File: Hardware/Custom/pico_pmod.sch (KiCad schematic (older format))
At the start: 31 parts, among them J1 Conn_02x06_Odd_Even, J2 Conn_02x06_Odd_Even, J3 Conn_02x06_Odd_Even, J4 USB_C_Receptacle_USB2.0, J5 Conn_01x04, SW1 SW_Push, SW2 SW_Push, U1 RP2040, U2 W25Q128JVS, U3 NCP1117-3.3_SOT223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

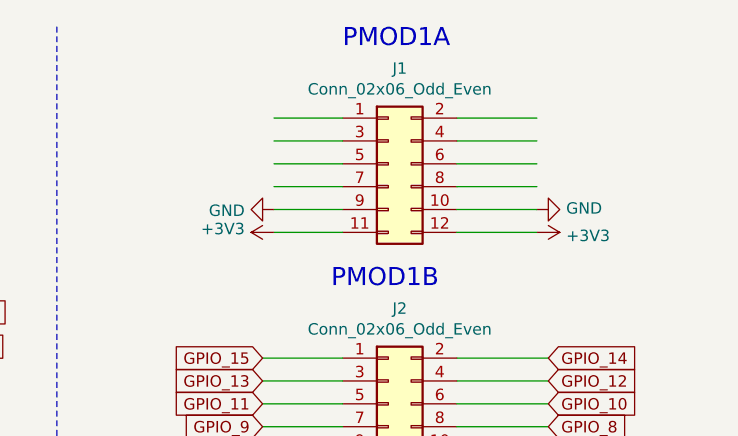
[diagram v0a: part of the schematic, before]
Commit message: Add connections to PMOD1A connector
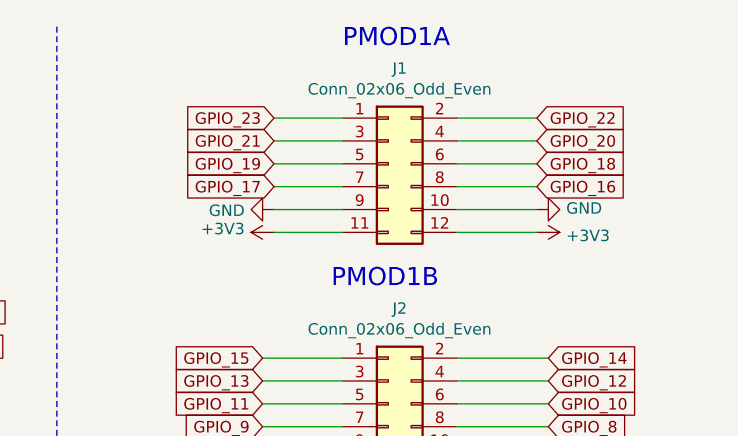
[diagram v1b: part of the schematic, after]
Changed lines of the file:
@@
 Wire Wire Line
 	9550 1950 9200 1950
+Text GLabel 10400 1200 2    50   Input ~ 0
+GPIO_16
+Text GLabel 10400 1100 2    50   Input ~ 0
+GPIO_18
+Text GLabel 10400 1000 2    50   Input ~ 0
+GPIO_20
+Text GLabel 10400 900  2    50   Input ~ 0
+GPIO_22
+Text GLabel 9250 900  0    50   Input ~ 0
+GPIO_23
+Text GLabel 9250 1000 0    50   Input ~ 0
+GPIO_21
+Text GLabel 9250 1100 0    50   Input ~ 0
+GPIO_19
+Text GLabel 9250 1200 0    50   Input ~ 0
+GPIO_17
 $EndSCHEMATC

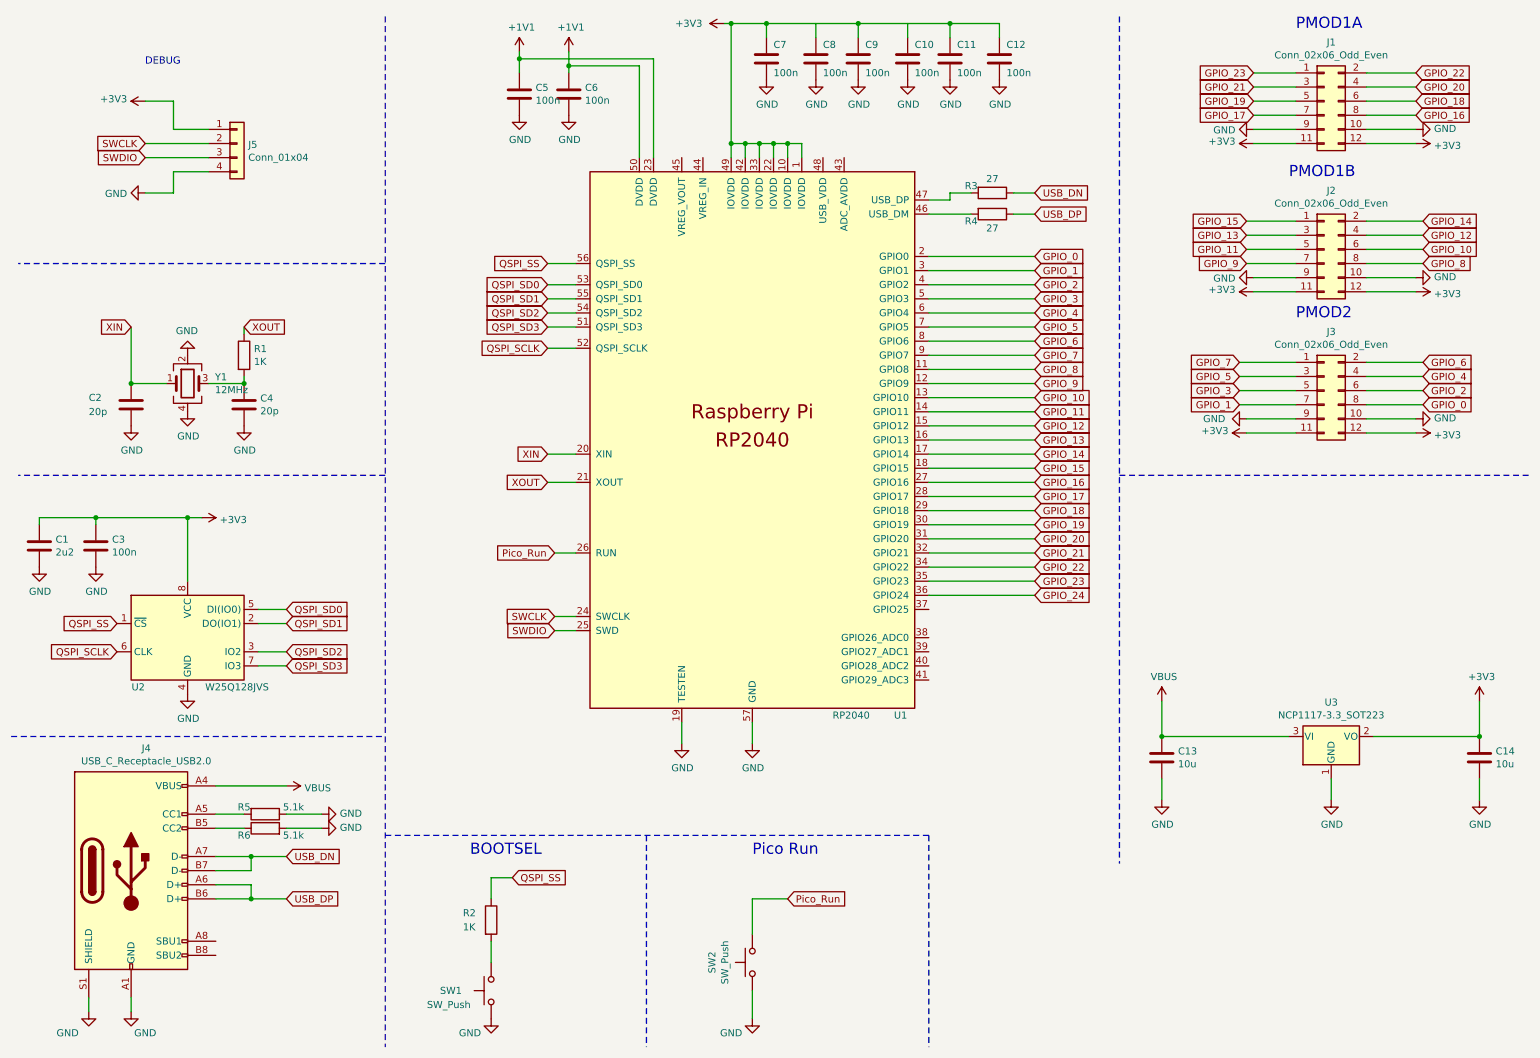
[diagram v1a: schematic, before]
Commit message: update with ground plane and LED's
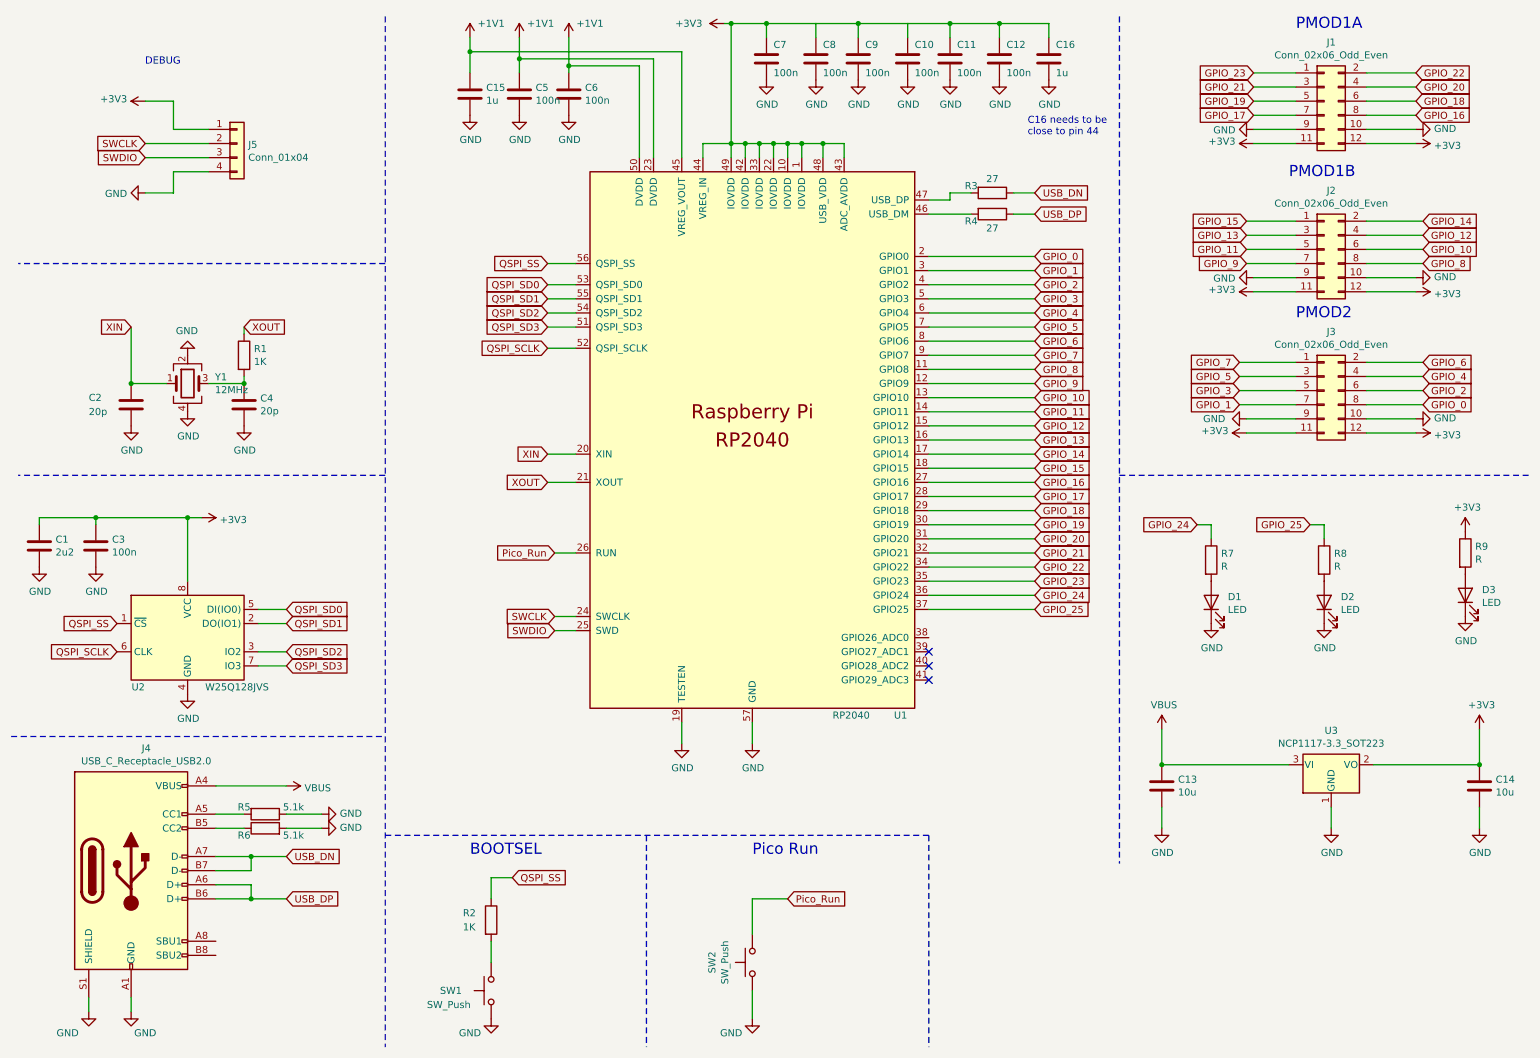
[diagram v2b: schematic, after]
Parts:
- added C15, C16: 1u, Capacitor_SMD:C_0603_1608Metric, symbol Device:C
- added D1, D2, D3: LED, LED_SMD:LED_0603_1608Metric, symbol Device:LED
- added R7, R8, R9: R, Resistor_SMD:R_0603_1608Metric, symbol Device:R
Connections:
- net +1V1: now also U1.45 (VREG_VOUT), C15.1
- net +3V3: now also U1.43 (ADC_AVDD), U1.44 (VREG_IN), U1.48 (USB_VDD), C16.1, R9.1
- net GND: now also C15.2, C16.2, D1.1 (K), D2.1 (K), D3.1 (K)
- net GPIO_24: now also R7.1
- net GPIO_25: now reaches U1.37 (GPIO25)
- net GPIO_25: now also R8.1
- new net: D1.2 (A), R7.2
- new net: D2.2 (A), R8.2
- new net: D3.2 (A), R9.2
- no-connect marks 0 -> 3
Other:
- note added: "C16 needs to be \nclose to pin 44"
- moved on the sheet: C13, C14, U3

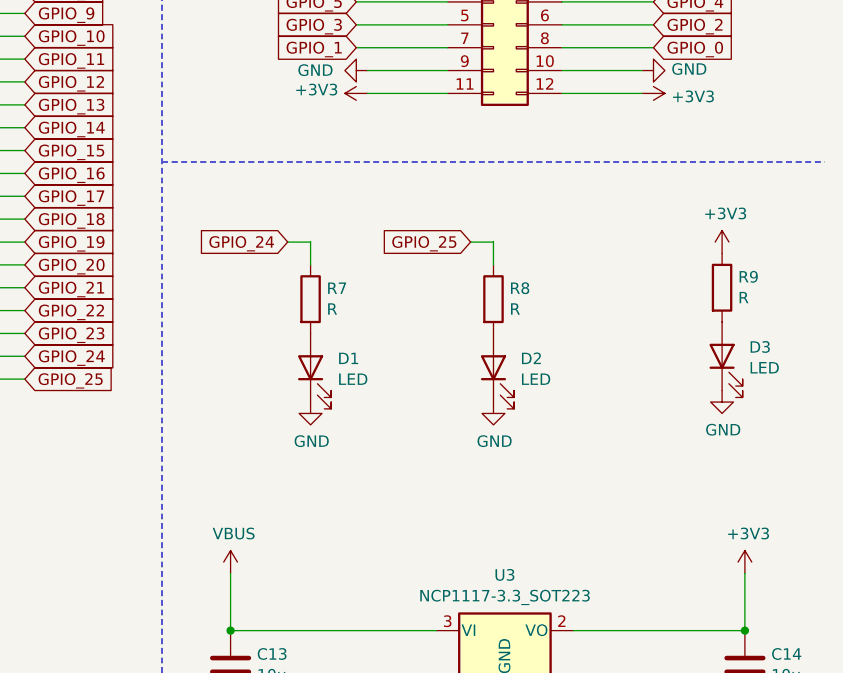
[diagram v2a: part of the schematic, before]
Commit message: Add lables to the Debug Port
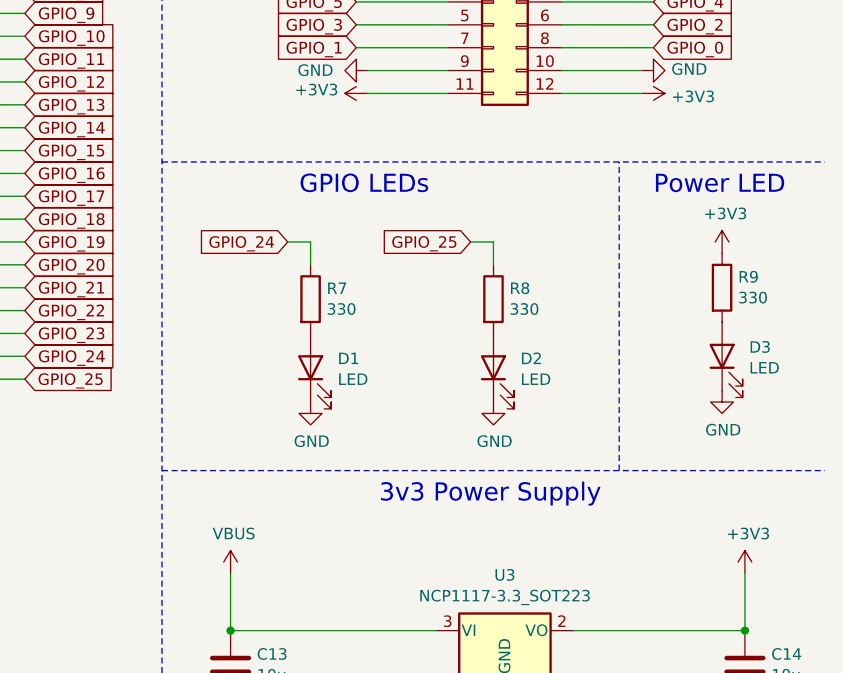
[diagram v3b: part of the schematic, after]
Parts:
- R7, R8, R9: value R -> 330
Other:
- note added: "3v3 Power Supply"
- note added: "GPIO LEDs"
- note added: "Power LED"
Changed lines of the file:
@@
 P 8950 4350
 F 0 "R7" H 9020 4396 50  0000 L CNN
-F 1 "R" H 9020 4305 50  0000 L CNN
+F 1 "330" H 9020 4305 50  0000 L CNN
 F 2 "Resistor_SMD:R_0603_1608Metric" V 8880 4350 50  0001 C CNN
 F 3 "~" H 8950 4350 50  0001 C CNN
@@
 P 9750 4350
 F 0 "R8" H 9820 4396 50  0000 L CNN
-F 1 "R" H 9820 4305 50  0000 L CNN
+F 1 "330" H 9820 4305 50  0000 L CNN
 F 2 "Resistor_SMD:R_0603_1608Metric" V 9680 4350 50  0001 C CNN
 F 3 "~" H 9750 4350 50  0001 C CNN
@@
 P 10750 4300
 F 0 "R9" H 10820 4346 50  0000 L CNN
-F 1 "R" H 10820 4255 50  0000 L CNN
+F 1 "330" H 10820 4255 50  0000 L CNN
 F 2 "Resistor_SMD:R_0603_1608Metric" V 10680 4300 50  0001 C CNN
 F 3 "~" H 10750 4300 50  0001 C CNN
@@
 NoConn ~ 6950 5100
 NoConn ~ 6950 5200
+Wire Notes Line
+	8300 5100 11200 5100
+Text Notes 9250 5250 0    79   ~ 0
+3v3 Power Supply
+Text Notes 8900 3900 0    79   ~ 0
+GPIO LEDs
+Text Notes 10450 3900 0    79   ~ 0
+Power LED
+Wire Notes Line
+	10300 5100 10300 3750
 $EndSCHEMATC
